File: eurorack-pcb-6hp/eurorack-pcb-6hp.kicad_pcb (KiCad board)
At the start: 2 copper layers, 99.8 x 108.3 mm, 0 parts

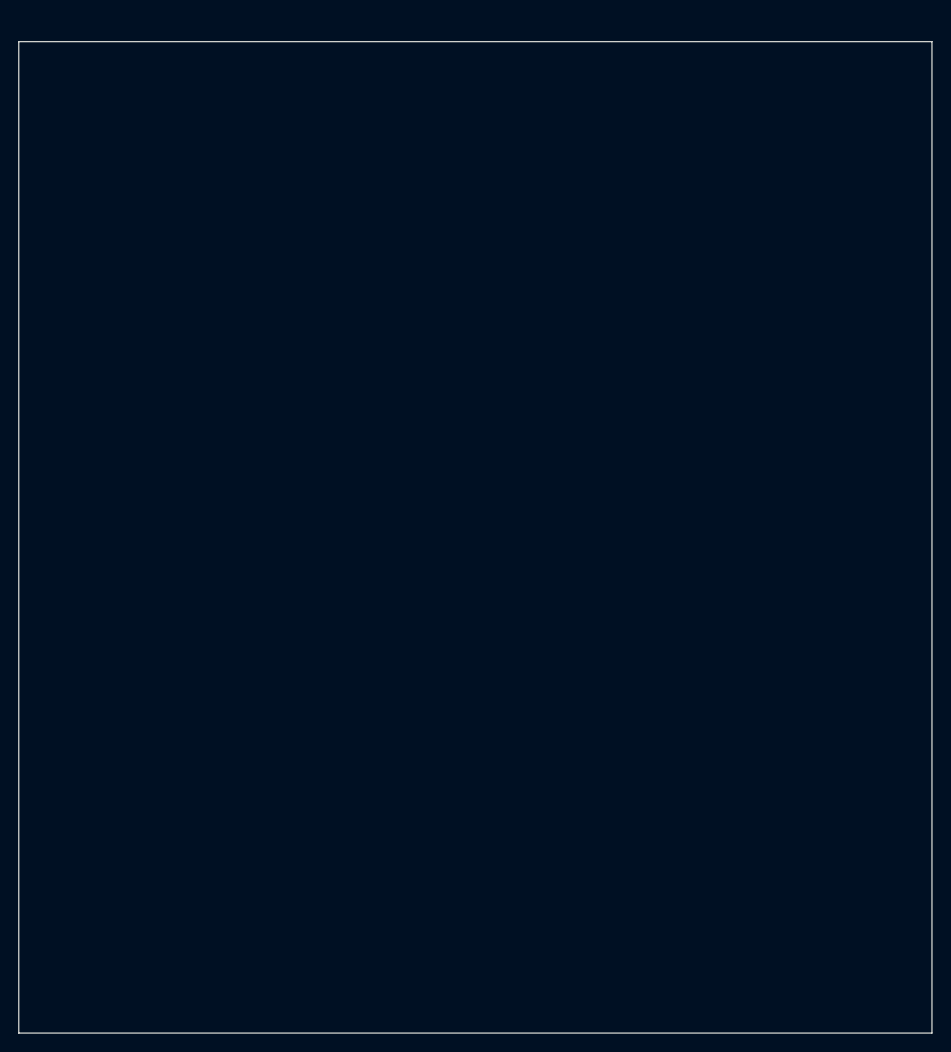
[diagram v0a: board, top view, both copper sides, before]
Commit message: Minor adjustments to PCB positioning. Moving everything into a single folder to be easier for kiCad to pick up all templates from user-template path
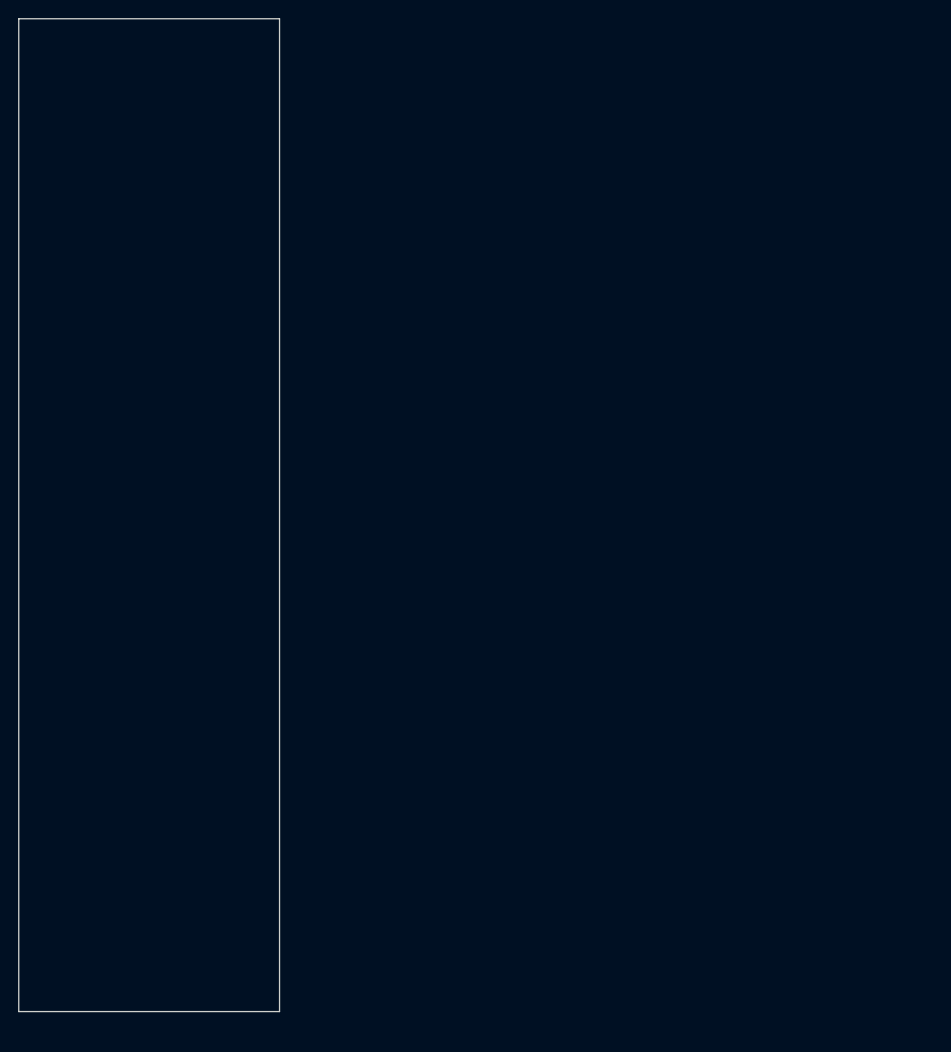
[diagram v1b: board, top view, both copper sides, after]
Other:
- board size 99.8 x 108.3 mm -> 28.5 x 108.5 mm
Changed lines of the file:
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@@
   )
   (net 0 "")
-  (gr_line (start 0.75 12.5) (end 0.75 120.85) (layer "Edge.Cuts") (width 0.1))
-  (gr_line (start 100.55 120.85) (end 100.55 12.5) (layer "Edge.Cuts") (width 0.1))
-  (gr_line (start 0.75 120.85) (end 100.55 120.85) (layer "Edge.Cuts") (width 0.1))
-  (gr_line (start 0.75 12.5) (end 100.55 12.5) (layer "Edge.Cuts") (width 0.1))
-  (gr_line (start 101.3 0) (end 101.3 128.5) (layer "User.1") (width 0.1))
+  (gr_line (start 0.75 10) (end 0.75 118.5) (layer "Edge.Cuts") (width 0.1))
+  (gr_line (start 29.25 118.5) (end 29.25 10) (layer "Edge.Cuts") (width 0.1))
+  (gr_line (start 0.75 118.5) (end 29.25 118.5) (layer "Edge.Cuts") (width 0.1))
+  (gr_line (start 0.75 10) (end 29.25 10) (layer "Edge.Cuts") (width 0.1))
+  (gr_line (start 30 0) (end 30 128.5) (layer "User.1") (width 0.1))
   (gr_line (start 0 128.5) (end 0 0) (layer "User.1") (width 0.1))
-  (gr_line (start 0 0) (end 101.3 0) (layer "User.1") (width 0.1))
-  (gr_line (start 101.3 128.5) (end 0 128.5) (layer "User.1") (width 0.1))
+  (gr_line (start 0 0) (end 30 0) (layer "User.1") (width 0.1))
+  (gr_line (start 30 128.5) (end 0 128.5) (layer "User.1") (width 0.1))
 )
